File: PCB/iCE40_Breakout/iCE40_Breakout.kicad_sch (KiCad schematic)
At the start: 0 parts

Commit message: Added FPGA associated power management
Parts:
- added C1, C11, C13, C3, C5, C7, C9: 4.7μF, symbol Device:C_Small
- added C10, C12, C14, C2, C4, C6, C8: 100nF, symbol Device:C_Small
- added C15, C17, C19: 1μF, symbol Device:C_Small
- added C16, C18, C20: 10μF, symbol Device:C_Small
- added U1: ICE40LP384-SG32, FPGA_Lattice_iCE40:QFNS32_LAT, symbol FPGA-Lattice-iCE40:ICE40LP384-SG32
- added U2, U5: MIC5504-3.3YM5, Package_TO_SOT_SMD:SOT-23-5, symbol Regulator_Linear:MIC5504-3.3YM5
- added U4: MIC5504-1.2YM5, Package_TO_SOT_SMD:SOT-23-5, symbol Regulator_Linear:MIC5504-1.2YM5
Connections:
- new net 1V2: C1.1, C2.1
- new net 3V3: C10.1, C11.1, C12.1, C13.1, C14.1, C3.1, C4.1, C5.1, C6.1, C7.1, C8.1, C9.1
- new net GND: C1.2, C10.2, C11.2, C12.2, C13.2, C14.2, C15.2, C16.2, C17.2, C18.2, C19.2, C2.2, C20.2, C3.2, C4.2, C5.2, C6.2, C7.2, C8.2, C9.2, U1.21 (GND), U1.3 (GND), U2.2 (GND), U4.2 (GND), U5.2 (GND)
- new net USB5V: C15.1, C17.1, C19.1, U2.1 (VIN), U4.1 (VIN), U4.3 (EN), U5.1 (VIN)
- new net VCC: C16.1, U1.25 (VCC), U4.5 (VOUT), U5.3 (EN)
- new net VCCIO/SPI: C18.1, U1.16 (VCC_SPI), U1.17 (VCCIO_1), U1.28 (VCCIO_0), U1.4 (VCCIO_3), U1.9 (VCCIO_2), U2.3 (EN), U5.5 (VOUT)
- new net VPP: C20.1, U1.24 (VPP_2V5), U2.5 (VOUT)
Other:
- note added: "1V2 Regulator"
- note added: "3V3 Regulator"
- note added: "FPGA Power"
- note added: "Sequenced to be after VCC, as per FPGA power up sequence"
- note added: "Sequenced to be after VCCSPI, as per FPGA power up sequence"
- note added: "X7R/X5R ceramic caps reccomended in datasheet"

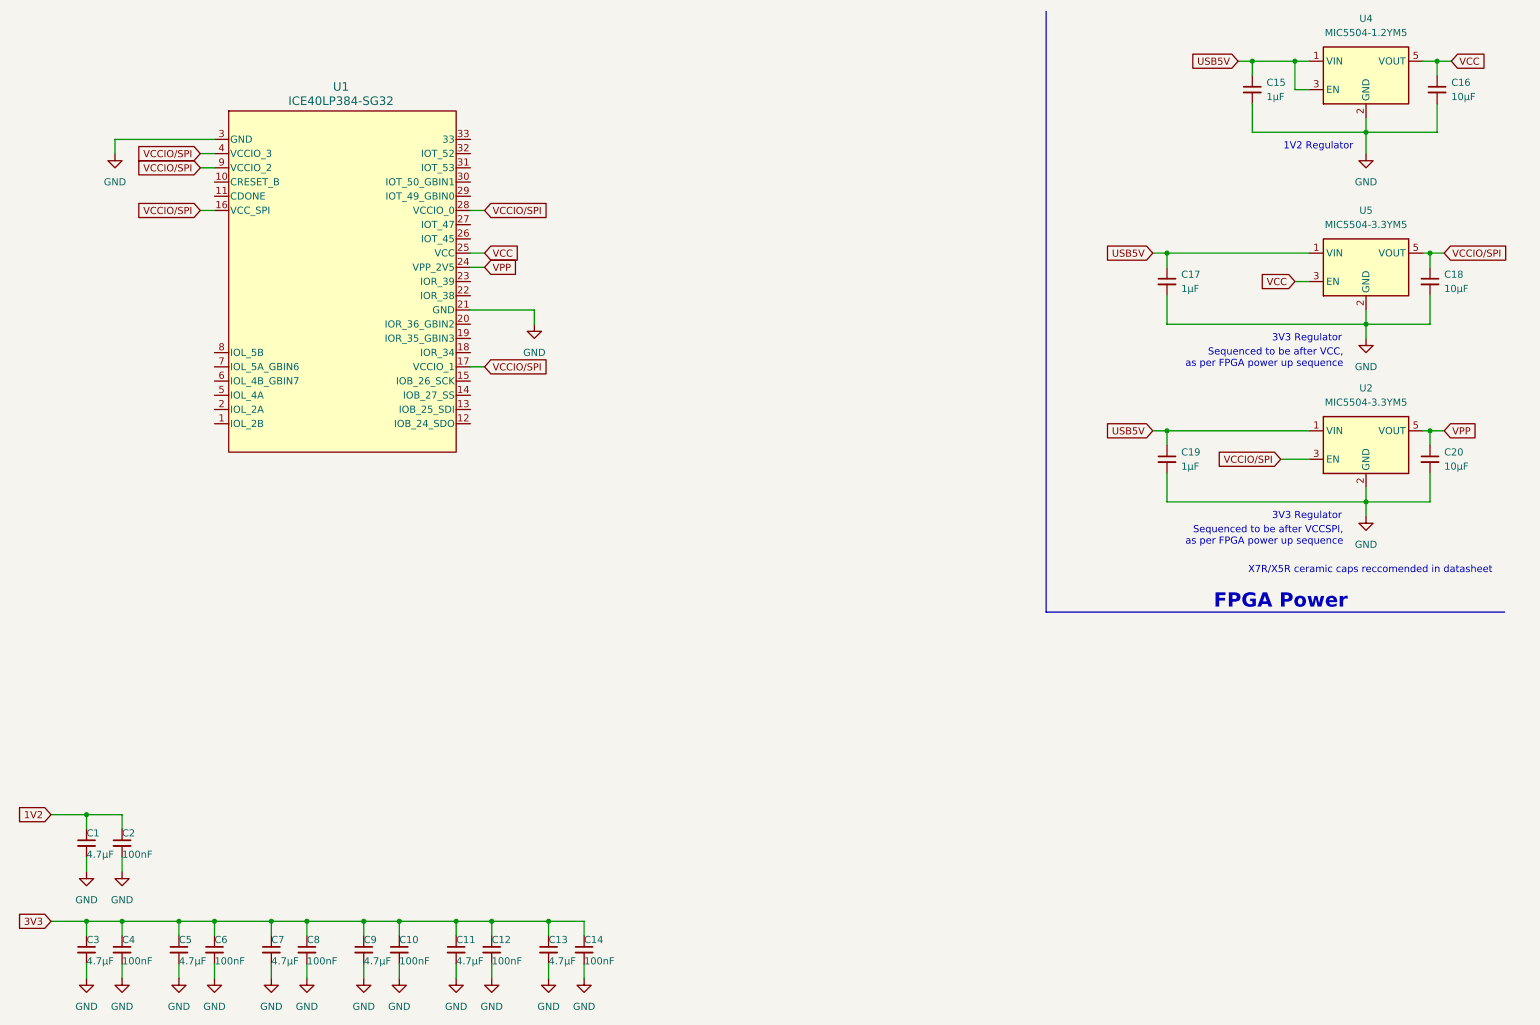
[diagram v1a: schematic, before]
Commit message: Moved FPGA and Power schematics to seperate sheets
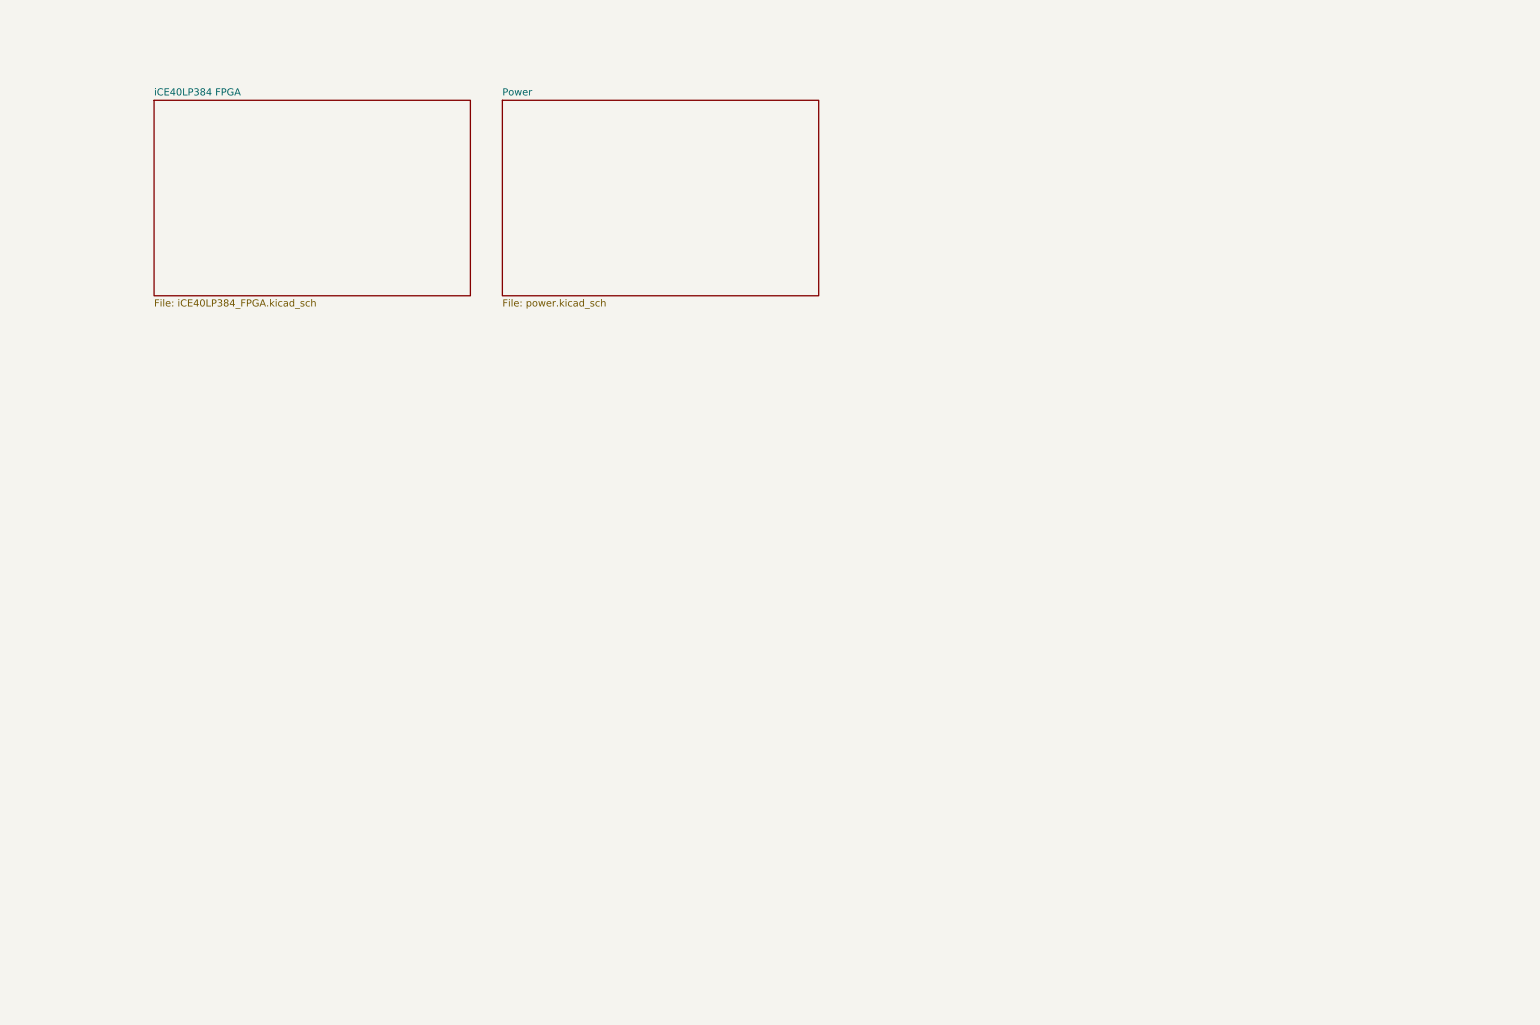
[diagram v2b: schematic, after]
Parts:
- removed C1, C11, C13, C3, C5, C7, C9: 4.7μF, symbol Device:C_Small
- removed C10, C12, C14, C2, C4, C6, C8: 100nF, symbol Device:C_Small
- removed C15, C17, C19: 1μF, symbol Device:C_Small
- removed C16, C18, C20: 10μF, symbol Device:C_Small
- removed U1: ICE40LP384-SG32, FPGA_Lattice_iCE40:QFNS32_LAT, symbol FPGA-Lattice-iCE40:ICE40LP384-SG32
- removed U2, U5: MIC5504-3.3YM5, Package_TO_SOT_SMD:SOT-23-5, symbol Regulator_Linear:MIC5504-3.3YM5
- removed U4: MIC5504-1.2YM5, Package_TO_SOT_SMD:SOT-23-5, symbol Regulator_Linear:MIC5504-1.2YM5
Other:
- added sheet Power (power.kicad_sch)
- added sheet iCE40LP384 FPGA (iCE40LP384_FPGA.kicad_sch)
- note removed: "1V2 Regulator"
- note removed: "3V3 Regulator"
- note removed: "FPGA Power"
- note removed: "Sequenced to be after VCC, as per FPGA power up sequence"
- note removed: "Sequenced to be after VCCSPI, as per FPGA power up sequence"
- note removed: "X7R/X5R ceramic caps reccomended in datasheet"

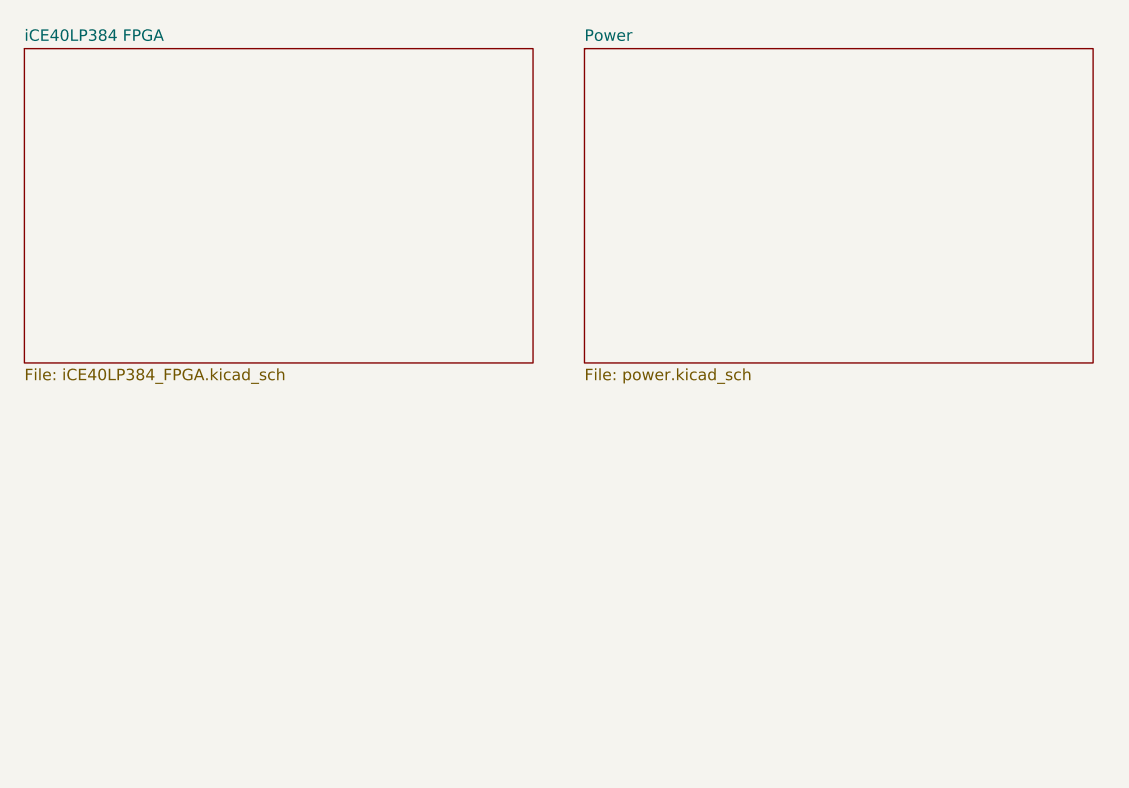
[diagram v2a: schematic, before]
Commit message: SPI flash for config storage
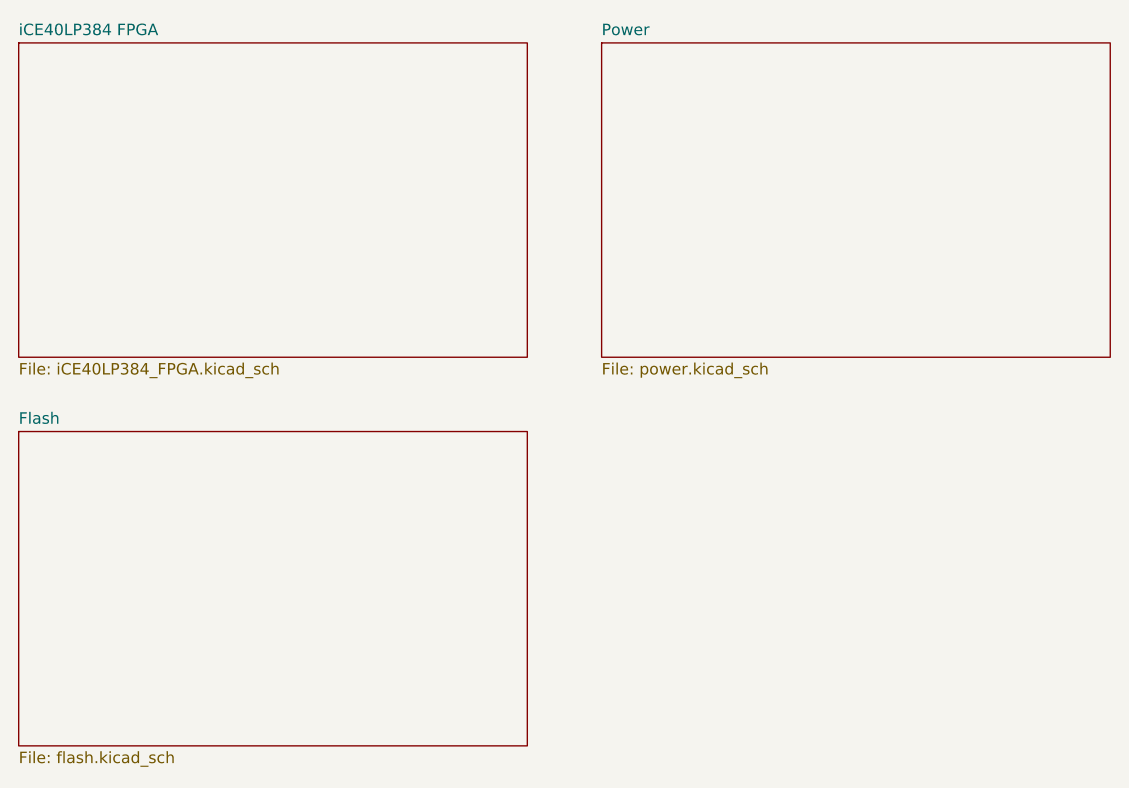
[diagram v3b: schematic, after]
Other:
- added sheet Flash (flash.kicad_sch)
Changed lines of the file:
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@@
 	(paper "A4")
 	(sheet
-		(at 102.235 29.845)
+		(at 104.14 29.21)
 		(size 56.515 34.925)
 		(exclude_from_sim no)
@@
 		)
 		(property "Sheetname" "Power"
-			(at 102.235 29.1334 0)
+			(at 104.14 28.4984 0)
 			(effects
 				(font
@@
 		)
 		(property "Sheetfile" "power.kicad_sch"
-			(at 102.235 65.3546 0)
+			(at 104.14 64.7196 0)
 			(effects
 				(font
@@
 	)
 	(sheet
-		(at 40.005 29.845)
+		(at 39.37 72.39)
+		(size 56.515 34.925)
+		(exclude_from_sim no)
+		(in_bom yes)
+		(on_board yes)
+		(dnp no)
+		(fields_autoplaced yes)
+		(stroke
+			(width 0.1524)
+			(type solid)
+		)
+		(fill
+			(color 0 0 0 0.0000)
+		)
+		(property "Sheetname" "Flash"
+			(at 39.37 71.6784 0)
+			(effects
+				(font
+					(size 1.27 1.27)
+				)
+				(justify left bottom)
+			)
+		)
+		(property "Sheetfile" "flash.kicad_sch"
+			(at 39.37 107.8996 0)
+			(effects
+				(font
+					(size 1.27 1.27)
+				)
+				(justify left top)
+			)
+		)
+		(instances
+			(project "iCE40_Breakout"
+				(path "/ce4d7974-ef38-4eea-8119-381c4298ef02"
+					(page "4")
+				)
+			)
+		)
+	)
+	(sheet
+		(at 39.37 29.21)
 		(size 56.515 34.925)
 		(exclude_from_sim no)
@@
 		)
 		(property "Sheetname" "iCE40LP384 FPGA"
-			(at 40.005 29.1334 0)
+			(at 39.37 28.4984 0)
 			(effects
 				(font
@@
 		)
 		(property "Sheetfile" "iCE40LP384_FPGA.kicad_sch"
-			(at 40.005 65.3546 0)
+			(at 39.37 64.7196 0)
 			(effects
 				(font
